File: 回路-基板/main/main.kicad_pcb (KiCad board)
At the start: 2 copper layers, 60 x 60 mm, 49 parts, among them J1 Conn_01x07_Pin, J2 Conn_01x08_Pin, J3 Conn_01x08_Pin, J4 Conn_01x08_Pin, J5 Conn_01x08_Pin, M1 Jumper_2_Small_Open, M2 Jumper_2_Small_Open, M3 Jumper_2_Small_Open, SW1 SW_Push, SW2 SW_Push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

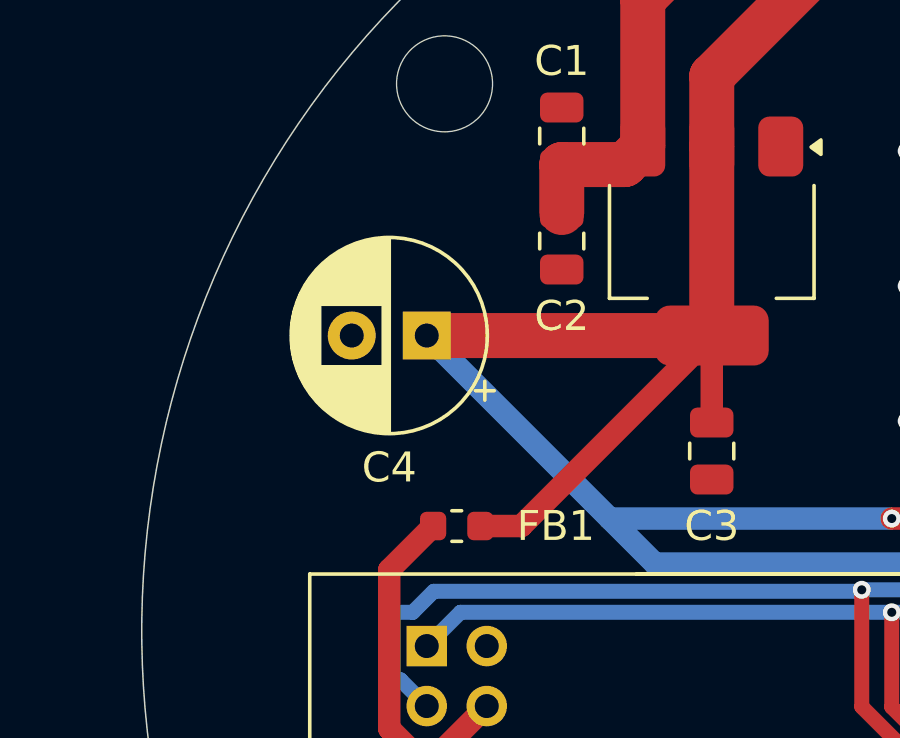
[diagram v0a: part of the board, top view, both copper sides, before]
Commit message: 電源用のLEDのつけ忘れを慌てて修正したよ
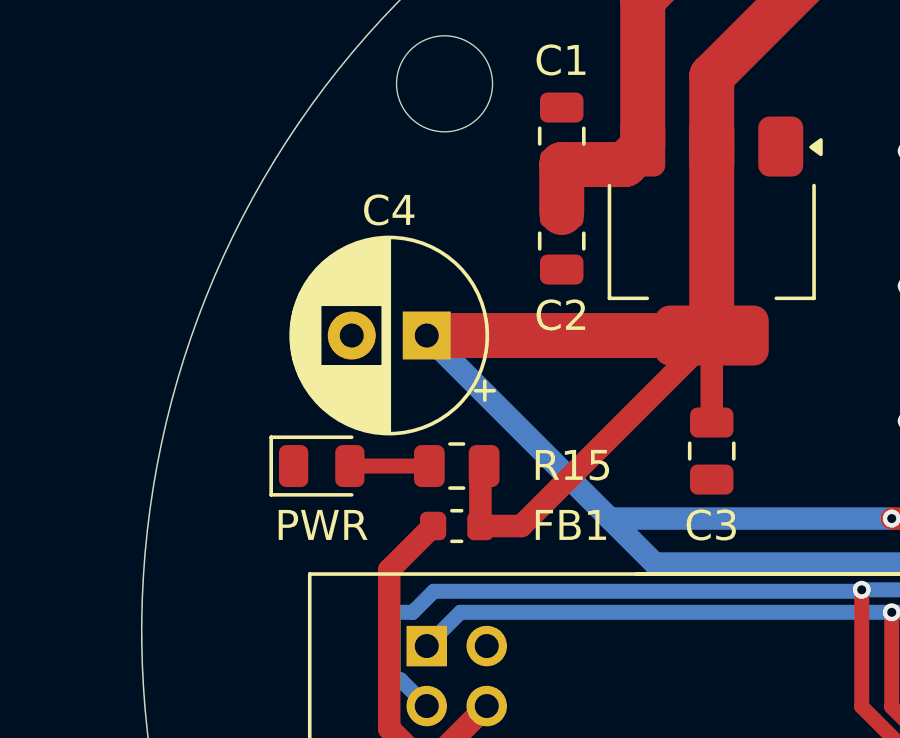
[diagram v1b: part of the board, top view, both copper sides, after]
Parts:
- added PWR: PWR, LED_SMD:LED_0805_2012Metric, F.Cu at (-24.0, -5.50)
- added R15: 1K, Resistor_SMD:R_0805_2012Metric, F.Cu at (-19.5, -5.50)
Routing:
- net Net-(D1-A): track 0.00 -> 2.65 mm
- net +3.3V: track 153.1 -> 155.2 mm

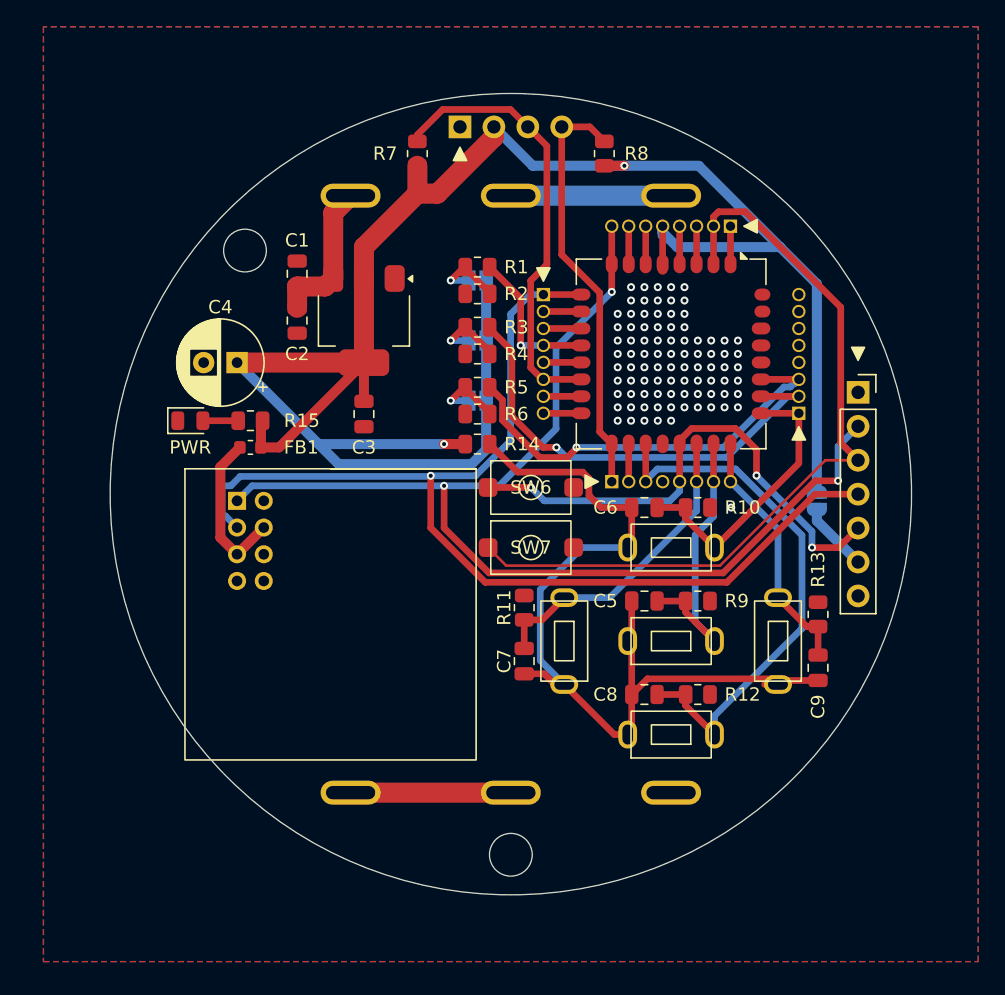
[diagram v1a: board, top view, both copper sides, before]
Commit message: 回路図とPCBを修正した
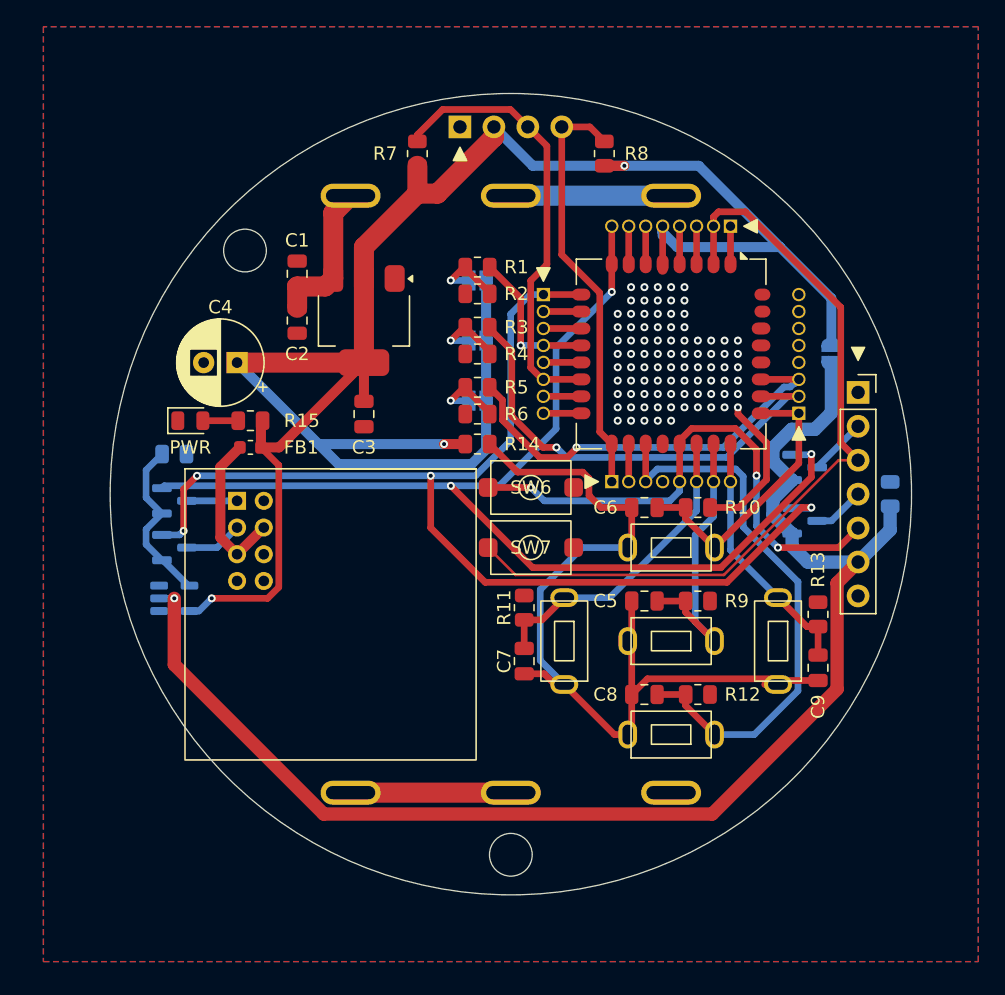
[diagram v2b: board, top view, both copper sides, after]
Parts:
- removed VBUS/+3.3V: Jumper_2_Small_Open, Jumper:SolderJumper-2_P1.3mm_Open_RoundedPad1.0x1.5mm
- added 3.3V        VBUS: Jumper_2_Small_Open, Jumper:SolderJumper-2_P1.3mm_Open_RoundedPad1.0x1.5mm, B.Cu at (24.0, -10.5)
- added NOT: 74AHC1G04, Package_TO_SOT_SMD:SOT-23-5, B.Cu at (-25.2, 7.80)
- added Q1: NMOS, Package_TO_SOT_SMD:SOT-23, B.Cu at (22.0, 2.00)
- added Q2: NMOS, Package_TO_SOT_SMD:SOT-23, B.Cu at (-25.2, 0.50)
- added Q3: NMOS, Package_TO_SOT_SMD:SOT-23, B.Cu at (22.0, -2.00)
- added Q4: NMOS, Package_TO_SOT_SMD:SOT-23, B.Cu at (-25.2, 4.00)
- added R17: 10K, Resistor_SMD:R_0805_2012Metric, B.Cu at (28.4, 0.00)
- added R18: 10K, Resistor_SMD:R_0805_2012Metric, B.Cu at (-25.2, -3.00)
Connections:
- J1 pad 2: 8 -> TX_W
- J1 pad 4: 9 -> RX_W
- J1 pad 6: Net-(J1-Pin_6) -> VBUS
- U4 pad 1: 8 -> TX_G
- U4 pad 3: 9 -> RX_G
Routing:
- net VBUS: track 0.00 -> 103.4 mm, vias 0 -> 1
- net VBUS-NOT: track 0.00 -> 12.8 mm
- net GND: track 0.00 -> 11.4 mm, vias 88 -> 87
- net +3.3V: track 155.2 -> 163.1 mm, vias 2 -> 3
- net Net-(J1-Pin_6): track 5.21 -> 0.00 mm
- net RX_G: track 0.00 -> 4.37 mm
- net TX_W: track 0.00 -> 4.35 mm
- net RX_W: track 0.00 -> 3.89 mm
- net TX_G: track 0.00 -> 3.75 mm
- net 9: track 82.4 -> 84.1 mm, vias 1 -> 4
- net 19: track 40.7 -> 42.2 mm
- net 21: track 38.7 -> 40.2 mm
- net 8: track 84.6 -> 83.8 mm
- net 2: track 59.7 -> 60.3 mm

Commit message: 回路図とPCBを修正してJLCPCB用のファイルを出力した
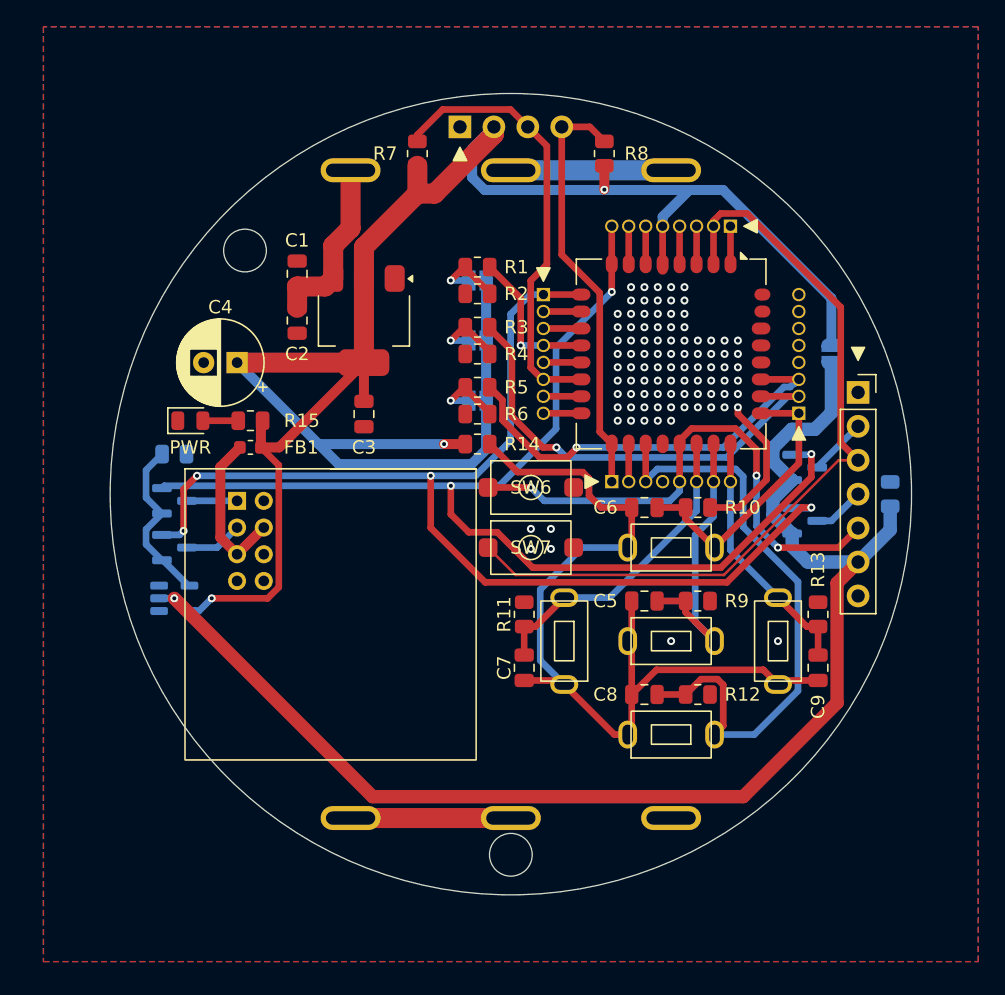
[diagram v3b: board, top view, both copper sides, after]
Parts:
- moved BT1 1.90 mm to (12.0, -24.2)
- moved BT2 1.90 mm to (0.00, 24.2)
- moved BT3 1.90 mm to (-12.0, -24.2)
- moved C7 0.50 mm to (1.00, 13.0)
- moved R11 0.50 mm to (1.00, 9.00)
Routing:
- net 19: track 42.2 -> 45.8 mm
- net VBUS: track 103.4 -> 100.0 mm
- net +3.3V: track 163.1 -> 160.9 mm
- net VCC: track 11.3 -> 13.2 mm
- net 8: track 83.8 -> 85.0 mm
- net Net-(C5-Pad1): track 67.9 -> 67.3 mm
- net GND: vias 87 -> 93

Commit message: 回路図とPCBを更新
GPSの電源のオンオフ式に切り替え
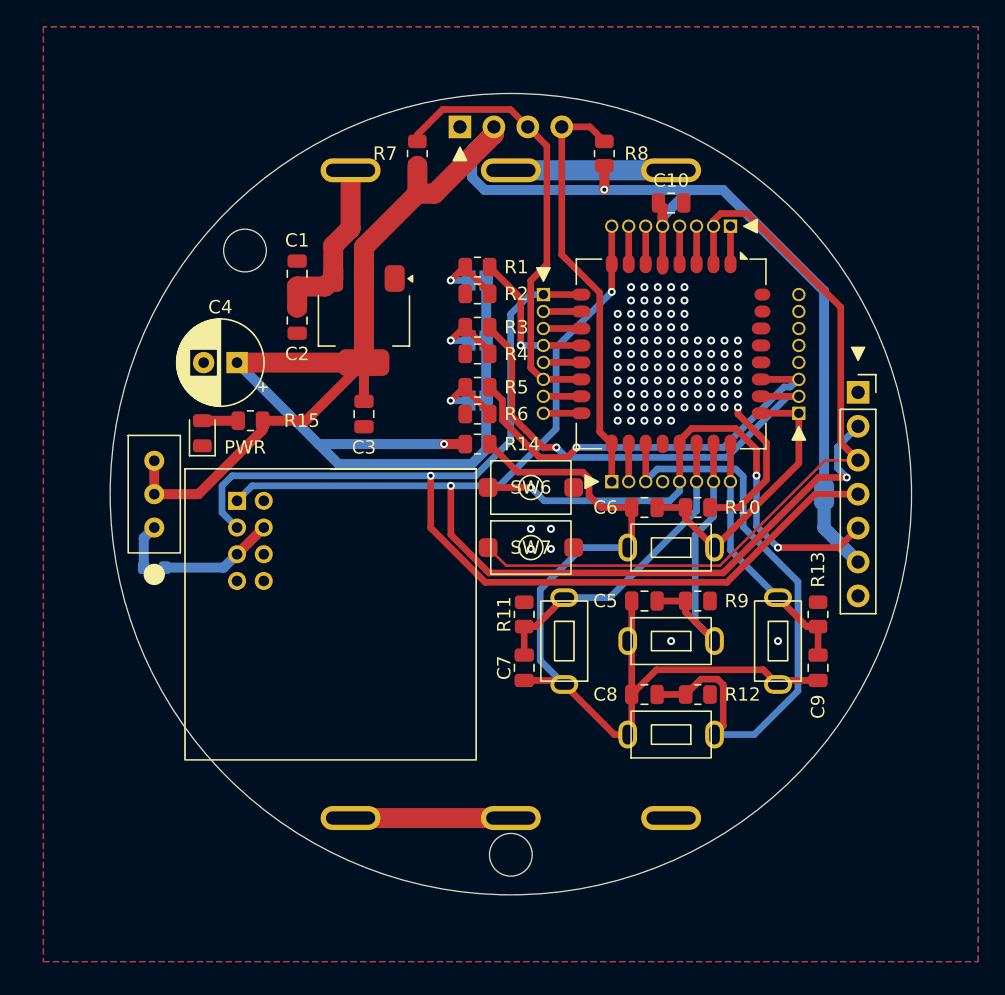
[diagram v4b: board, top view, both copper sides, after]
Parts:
- removed NOT: 74AHC1G04, Package_TO_SOT_SMD:SOT-23-5
- removed Q1, Q2, Q3, Q4: NMOS, Package_TO_SOT_SMD:SOT-23
- removed R17, R18: 10K, Resistor_SMD:R_0805_2012Metric
- added C10: 0.1uF, Capacitor_SMD:C_0805_2012Metric, F.Cu at (12.0, -21.8)
- added SW8: SW_SPDT, @2024-Power:SS12D01G4, F.Cu at (-26.7, 0.00)
- FB1: moved to B.Cu
- moved FB1 11.5 mm to (-26.7, 5.50), turned to 0 degrees
- moved 3.3V        VBUS 10.5 mm to (23.4, 0.00)
- moved PWR 1.30 mm to (-23.1, -4.56), turned to 90 degrees
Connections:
- FB1 pad 1: +3.3V -> GPS_PWR
- J1 pad 2: TX_W -> 8
- J1 pad 4: RX_W -> 9
- U4 pad 1: TX_G -> 8
- U4 pad 3: RX_G -> 9
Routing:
- net VBUS: track 100.0 -> 5.49 mm, vias 1 -> 0
- net VBUS-NOT: track 12.8 -> 0.00 mm
- net RX_G: track 4.37 -> 0.00 mm
- net TX_W: track 4.35 -> 0.00 mm
- net +3.3V: track 160.9 -> 164.9 mm, vias 3 -> 2
- net RX_W: track 3.89 -> 0.00 mm
- net TX_G: track 3.75 -> 0.00 mm
- net GPS_PWR: track 0.00 -> 3.33 mm
- net Net-(U4-BATT): track 12.0 -> 8.66 mm
- net 9: track 84.1 -> 82.3 mm, vias 4 -> 1
- net 2: track 60.0 -> 59.4 mm

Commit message: 基板外形を更新したPCBを製造用ファイルに出力した
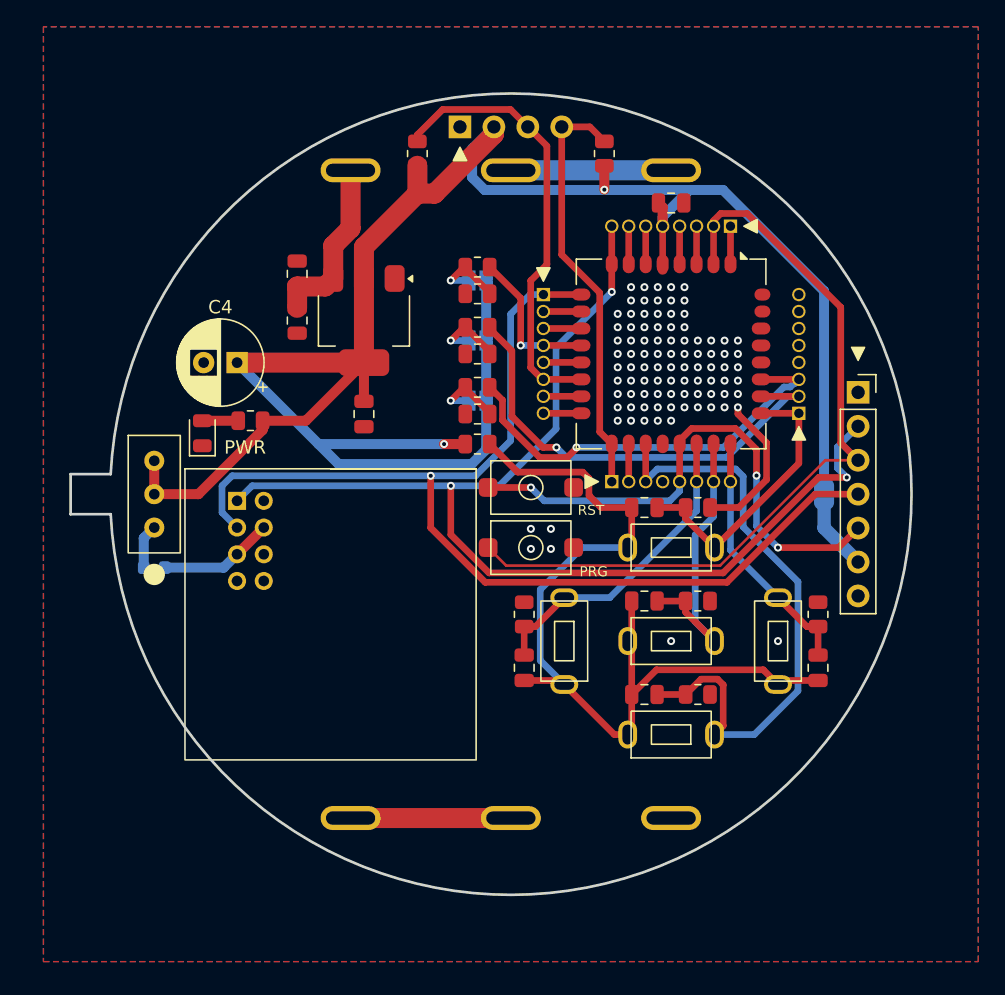
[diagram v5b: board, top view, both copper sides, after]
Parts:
- removed REF** (x2): MountingHole_3.2mm_M3, MountingHole:MountingHole_3.2mm_M3
- renumbered SW7 to PRG, SW6 to RST
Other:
- board size 60 x 60 mm -> 63 x 60 mm

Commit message: 基板関連色々やった
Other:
- board size 63 x 60 mm -> 63 x 63 mm
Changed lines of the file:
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@@
 		(layer "F.SilkS")
 	)
-	(gr_line
-		(start -32.962477 1.5)
-		(end -32.962477 -1.5)
+	(gr_arc
+		(start 1.967213 -29.935432)
+		(mid 22.558577 -19.776517)
+		(end 29.935432 1.967213)
 		(stroke
 			(width 0.2)
@@
 	)
 	(gr_arc
-		(start -29.962476 -1.5)
-		(mid 29.999999 0)
-		(end -29.962475 1.5)
+		(start -32.962477 -1)
+		(mid -32.816029 -1.353545)
+		(end -32.462477 -1.5)
 		(stroke
 			(width 0.2)
@@
 	)
 	(gr_line
-		(start -29.962475 1.5)
-		(end -32.962477 1.5)
+		(start -30.434356 -1.5)
+		(end -32.462477 -1.5)
 		(stroke
 			(width 0.2)
@@
 	)
 	(gr_line
-		(start -32.962477 -1.5)
-		(end -29.962476 -1.5)
+		(start 1 -32.962477)
+		(end -1.004795 -32.962477)
+		(stroke
+			(width 0.2)
+			(type default)
+		)
+		(layer "Edge.Cuts")
+	)
+	(gr_arc
+		(start 1 -32.962477)
+		(mid 1.353545 -32.816029)
+		(end 1.5 -32.462477)
+		(stroke
+			(width 0.2)
+			(type default)
+		)
+		(layer "Edge.Cuts")
+	)
+	(gr_arc
+		(start -29.935432 -1.967213)
+		(mid -21.213204 -21.213204)
+		(end -1.967213 -29.935432)
+		(stroke
+			(width 0.2)
+			(type default)
+		)
+		(layer "Edge.Cuts")
+	)
+	(gr_arc
+		(start -1.5 -30.4344)
+		(mid -1.635033 -30.092602)
+		(end -1.967213 -29.935432)
+		(stroke
+			(width 0.2)
+			(type default)
+		)
+		(layer "Edge.Cuts")
+	)
+	(gr_arc
+		(start 29.935432 1.967213)
+		(mid 0 30)
+		(end -29.935432 1.967213)
+		(stroke
+			(width 0.2)
+			(type default)
+		)
+		(layer "Edge.Cuts")
+	)
+	(gr_line
+		(start -32.962477 -1)
+		(end -32.962477 1.00469)
+		(stroke
+			(width 0.2)
+			(type default)
+		)
+		(layer "Edge.Cuts")
+	)
+	(gr_arc
+		(start -30.4344 1.5)
+		(mid -30.092602 1.635033)
+		(end -29.935432 1.967213)
+		(stroke
+			(width 0.2)
+			(type default)
+		)
+		(layer "Edge.Cuts")
+	)
+	(gr_line
+		(start -32.4625 1.5)
+		(end -30.4344 1.5)
+		(stroke
+			(width 0.2)
+			(type default)
+		)
+		(layer "Edge.Cuts")
+	)
+	(gr_arc
+		(start -1.5 -32.4625)
+		(mid -1.355245 -32.814354)
+		(end -1.004795 -32.962477)
+		(stroke
+			(width 0.2)
+			(type default)
+		)
+		(layer "Edge.Cuts")
+	)
+	(gr_line
+		(start 1.5 -30.434356)
+		(end 1.5 -32.462477)
+		(stroke
+			(width 0.2)
+			(type default)
+		)
+		(layer "Edge.Cuts")
+	)
+	(gr_arc
+		(start -29.935432 -1.967213)
+		(mid -30.092588 -1.635023)
+		(end -30.434356 -1.5)
+		(stroke
+			(width 0.2)
+			(type default)
+		)
+		(layer "Edge.Cuts")
+	)
+	(gr_arc
+		(start 1.967213 -29.935432)
+		(mid 1.635023 -30.092588)
+		(end 1.5 -30.434356)
+		(stroke
+			(width 0.2)
+			(type default)
+		)
+		(layer "Edge.Cuts")
+	)
+	(gr_arc
+		(start -32.4625 1.5)
+		(mid -32.814391 1.355208)
+		(end -32.962477 1.00469)
+		(stroke
+			(width 0.2)
+			(type default)
+		)
+		(layer "Edge.Cuts")
+	)
+	(gr_line
+		(start -1.5 -32.4625)
+		(end -1.5 -30.4344)
 		(stroke
 			(width 0.2)
@@
 	)
 	(group ""
-		(members "5b0e7101-af27-4375-adf4-d4f7e8126fe0" "6106658a-c8cd-4937-8db4-6a7645999039"
-			"6bdb15ae-44e8-462c-84d3-d6a422588827" "b942df8c-f8d6-4a23-88a3-342d41cade1d"
+		(members "22eba148-ecb8-4af1-84a2-3671ab316bbc" "28677f71-f918-428e-8951-7489588fa970"
+			"30b18946-49bd-4c90-acdd-2f0545d76cb0" "317997f5-1e7d-4396-a8f5-ea28c372f129"
+			"52e2f6f1-c2bd-48d2-8413-fa733dd2ee44" "54de99ce-7baf-4809-9e2d-a0c8345e2827"
+			"5526e115-8e32-476e-a883-6bce5dc561fe" "5e18ec7a-75ed-4ca2-b2ef-ca469fee5d7a"
+			"6d51ea9e-64b0-4dd0-a876-8cff49f3dc93" "86fae30e-855d-475d-a81a-4e0a7b3fc407"
+			"92bf97ba-9ad2-4ef6-9433-4ed0f360f754" "93163d0d-3a21-4e40-a977-0a0fd4b1fa3e"
+			"aaf5d20a-ba35-4501-9d1e-e25c7eb84191" "d3f144cf-8035-40ad-b807-5e1b350bffda"
+			"dcd26f5d-c39f-43eb-ace9-130209412a39" "e72acc82-bd71-47ad-a6e2-d4b3d6105890"
+			"fb79628b-2192-4a9a-b396-ca430f938576"
 		)
 	)

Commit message: ピンのテストプログラムと基板の更新版PCB
PCBのDRよろしくー
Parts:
- added DIO13: LED, LED_SMD:LED_0805_2012Metric, F.Cu at (0.51, 19.0)
- added R16: 330, Resistor_SMD:R_0805_2012Metric, F.Cu at (0.51, 17.0)
- moved C10 6.99 mm to (5.01, -21.8), turned to -90 degrees
- moved BT1 0.49 mm to (11.5, -24.2)
- moved BT3 0.49 mm to (-12.5, -24.2)
- moved C1 0.49 mm to (-16.5, -16.5)
- moved SW4 0.49 mm to (11.5, 18.0)
- moved 3.3V        VBUS 0.49 mm to (23.0, 0.04)
- moved C6 0.49 mm to (9.51, 1.04)
- moved J1 0.49 mm to (25.5, -7.58)
- moved R10 0.49 mm to (13.5, 1.04)
- moved SW8 0.49 mm to (-27.2, 0.04)
- moved C2 0.49 mm to (-16.5, -13.0)
- moved C3 0.49 mm to (-11.5, -5.96)
- moved C4 0.49 mm to (-21.0, -9.81)
- moved C5 0.49 mm to (9.51, 8.04)
- moved C8 0.49 mm to (9.51, 15.0)
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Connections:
- C5 pad 2: 23 -> 18
- C7 pad 2: 22 -> 16
- R11 pad 2: 22 -> 16
- R9 pad 2: 23 -> 18
- SW1 pad 1: 23 -> 18
- SW3 pad 1: 22 -> 16
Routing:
- net 16: track 2.83 -> 68.5 mm, vias 0 -> 1
- net 15: track 2.83 -> 39.5 mm
- net 18: track 2.83 -> 37.7 mm
- net 22: track 23.1 -> 2.83 mm
- net 23: track 22.0 -> 2.83 mm
- net +3.3V: track 164.9 -> 152.1 mm
- net GND: track 11.4 -> 1.12 mm, vias 93 -> 14
- net 27: track 31.5 -> 28.7 mm
- net 9: track 82.3 -> 84.4 mm, vias 1 -> 2
- net Net-(D2-A): track 0.00 -> 2.01 mm
- net 2: track 59.4 -> 61.0 mm, vias 0 -> 4
- net 17: track 31.8 -> 32.9 mm
- net 12: track 11.4 -> 10.4 mm
- net VCC: track 13.2 -> 13.8 mm
- net 21: track 40.2 -> 39.6 mm
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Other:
- board text added: "+"
- board text added: "1"
- board text added: "17"
- board text added: "25"
- board text added: "9"
- board text added: "CL"
- board text added: "DA"
- board text added: "GND"
